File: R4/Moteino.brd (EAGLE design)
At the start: 33.3 x 23.1 mm, 22 parts, among them IC3 MCP1703CB, X1 16 MHz

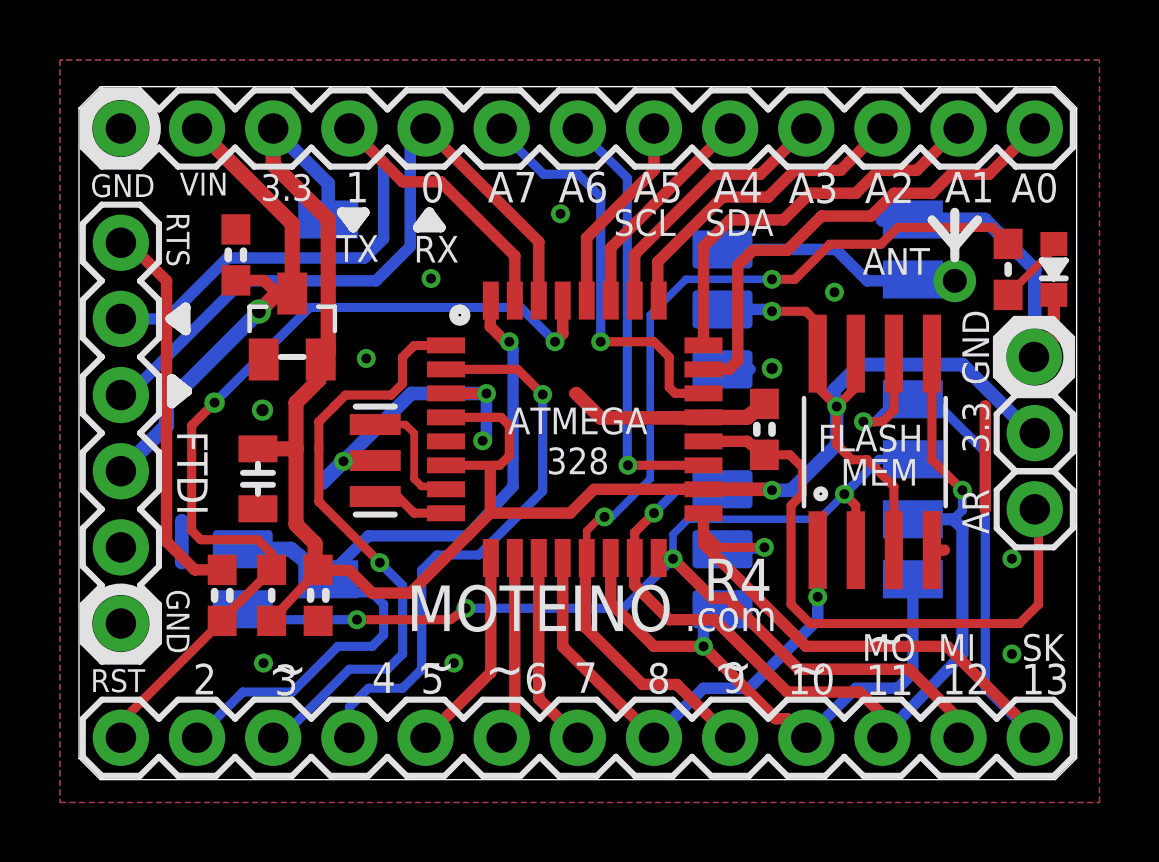
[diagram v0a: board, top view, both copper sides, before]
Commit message: Update Eagle files, add schematic PDFs
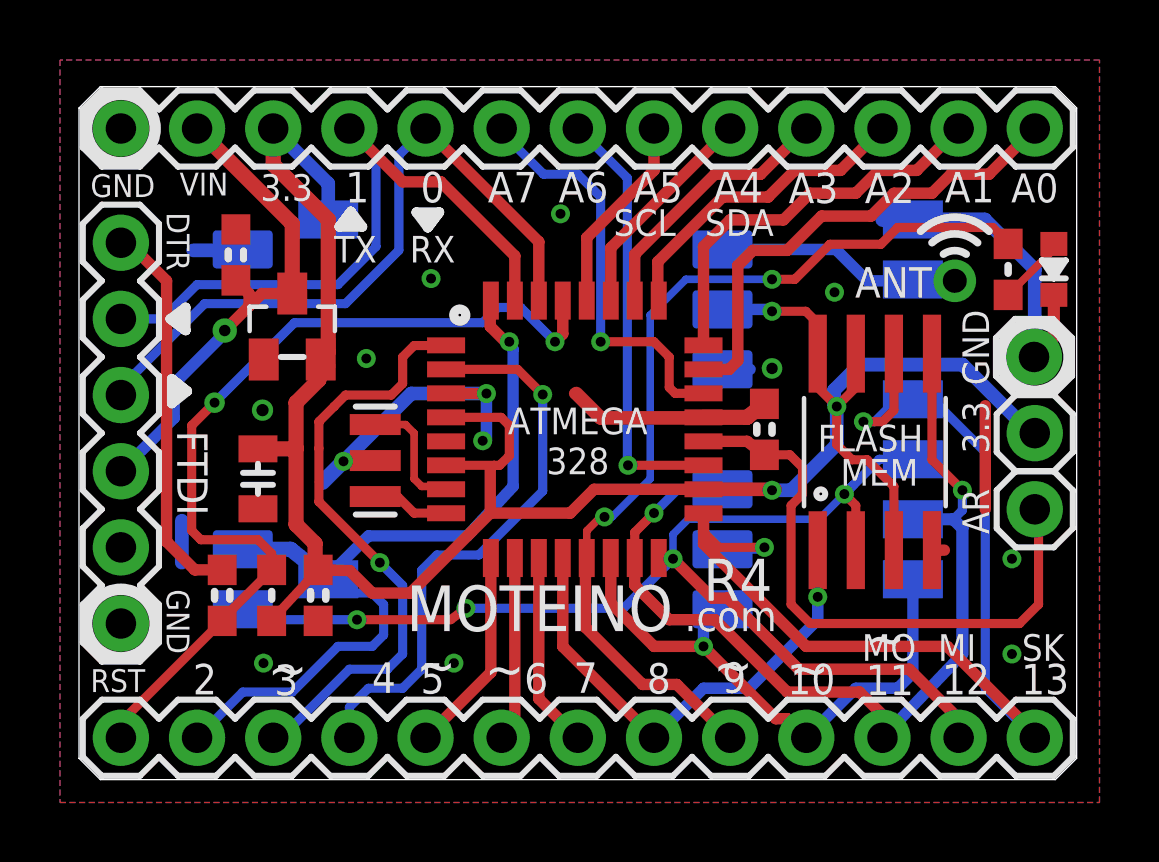
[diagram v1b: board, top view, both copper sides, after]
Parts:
- renumbered U$6 to W25X40CLSNIG-ND
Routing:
- net GND: track 36.4 -> 37.9 mm
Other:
- board text added: "DTR"
- board text added: "XXXXXXXXXXXX"
- board text removed: "RTS"
